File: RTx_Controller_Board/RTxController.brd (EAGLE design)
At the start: 101.6 x 85.5 mm, 79 parts, among them U1 TPD4S014, X3 MINI-USB-32005-301

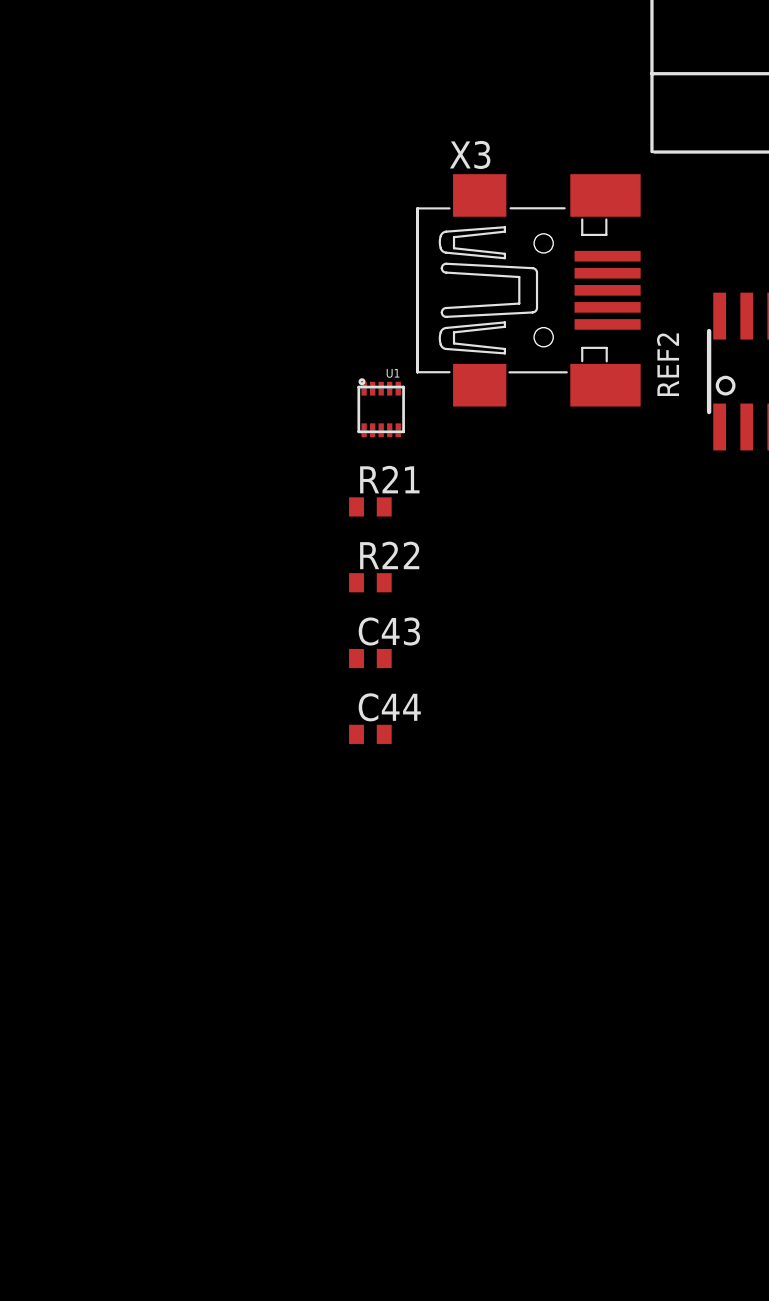
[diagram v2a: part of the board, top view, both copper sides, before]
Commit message: Initial check-in of datasheet for USB ESD protection (better component selected). Updated USB in hardware to incorperate new esd chip.
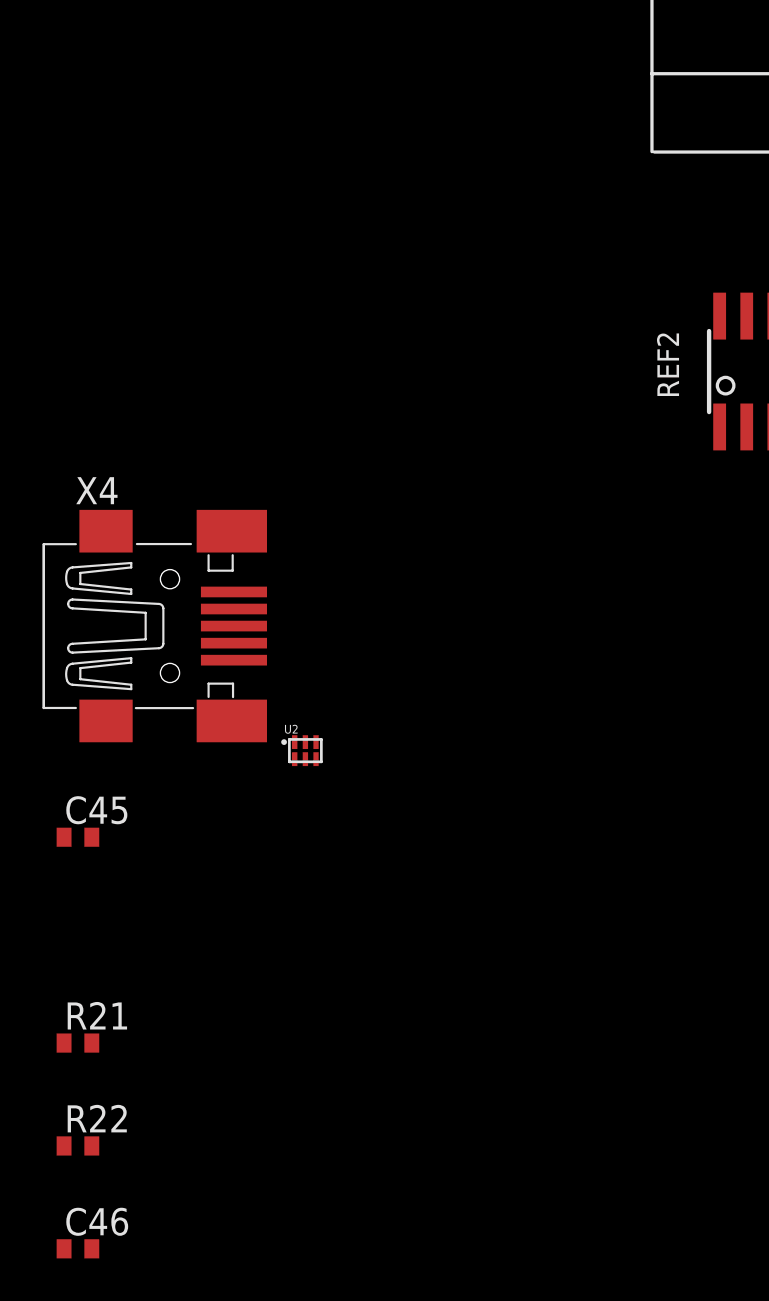
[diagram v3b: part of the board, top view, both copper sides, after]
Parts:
- removed C43, C44: 10u, rcl:C0402
- removed U1: TPD4S014, rtx:TPD4S014
- removed X3: MINI-USB-32005-301, con-cypressindustries:32005-301
- added C45, C46: 10u, rcl:C0402
- added U2: TPD4S012, rtx:TPD4S012
- added X4: MINI-USB-32005-301, con-cypressindustries:32005-301
- moved R22 29.8 mm to (-26.7, -142.5)
- moved R21 28.6 mm to (-26.7, -137.7)
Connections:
- removed net PA9/VBUS: C44.1, U1.1
- new net PA10/ID: U2.3, X4.4
- new net PA9/BBUS: C45.1, C46.1, U2.6, X4.1
- net +5V: no longer C43.1, U1.9, X3.1
- net D+: now also R22.1, U2.1, X4.2; no longer R21.1, U1.7, X3.2
- net D-: now also R21.1, U2.2, X4.3; no longer R22.1, U1.6, X3.3
- net GND: now also C45.2, C46.2, U2.4, X4.5; no longer C43.2, C44.2, U1.5, U1.8, X3.4, X3.5
- net PA11/D-: now also R21.2; no longer R22.2
- net PA12/D+: now also R22.2; no longer R21.2

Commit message: Development of Ethernet PHY.
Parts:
- added C43, C47: 0.1uf 100v, motorFeedback:C0805K
- added C49: 0.1uf, motorFeedback:C0805K
- added D1: SMAJ58A, diode:SMBJ
- added D2: MMBD6050LT1SOT23, motorFeedback:SOT23-TO-236
- added F1: 1A, special:FUSE
- added IC1: LTC4263, motorFeedback:S14-NARROW
- added IC2: TLK110", motorFeedback:LQFP48
- added L1: 10mH, 21mA, motorFeedback:0204V
- added LED1: (no value), motorFeedback:LED5MM
- added R_LED: 1k, motorFeedback:R0603
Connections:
- new net 48VDC+: C43.1, D1.C, D2.3, F1.1, IC1.11, LED1.A
- new net 48VDC-: C43.2, C49.2, IC1.2, IC1.3, IC1.4, IC1.5, IC1.6, IC1.7
- new net AGND: IC2.19
- new net AGND_: IC2.15
- new net AVDD33: IC2.22
- new net DGND: IC2.36
- new net IOGND: IC2.47
- new net IOGND_: IC2.35
- new net N$15: C49.1, IC1.12, IC1.13, IC1.14
- new net N$23: L1.2, LED1.K
- new net N$24: D2.1, L1.1, R_LED.2
- new net N$25: IC1.1, R_LED.1
- new net PORT_MAGNETICS+: C47.1, F1.2
- new net PORT_MAGNETICS-: C47.2, D1.A, IC1.10, IC1.9
- new net VDD_IO: IC2.48
- new net VDD_IO_: IC2.32
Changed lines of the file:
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@@
 <layer number="97" name="Info" color="7" fill="1" visible="no" active="no"/>
 <layer number="98" name="Guide" color="6" fill="1" visible="no" active="no"/>
+<layer number="99" name="SpiceOrder" color="5" fill="1" visible="no" active="no"/>
 <layer number="100" name="Muster" color="7" fill="1" visible="no" active="no"/>
 <layer number="101" name="Patch_Top" color="12" fill="4" visible="yes" active="yes"/>
@@
 <element name="R22" library="rcl" package="R0402" value="22" x="-26.67" y="-142.494"/>
 <element name="C46" library="rcl" package="C0402" value="10u" x="-26.67" y="-147.32"/>
+<element name="IC1" library="motorFeedback" package="S14-NARROW" value="LTC4263" x="-32.258" y="-187.96"/>
+<element name="IC2" library="motorFeedback" package="LQFP48" value="TLK110&quot;" x="-41.656" y="-187.706"/>
+<element name="D1" library="diode" package="SMBJ" value="SMAJ58A" x="-52.324" y="-190.246"/>
+<element name="F1" library="special" package="FUSE" value="1A" x="-41.656" y="-200.406"/>
+<element name="C47" library="motorFeedback" package="C0805K" value="0.1uf 100v" x="-53.594" y="-208.534"/>
+<element name="C49" library="motorFeedback" package="C0805K" value="0.1uf" x="-53.594" y="-218.186"/>
+<element name="L1" library="motorFeedback" package="0204V" value="10mH, 21mA" x="-52.578" y="-223.52"/>
+<element name="LED1" library="motorFeedback" package="LED5MM" value="" x="-51.816" y="-228.346"/>
+<element name="R_LED" library="motorFeedback" package="R0603" value="1k" x="-53.594" y="-233.934"/>
+<element name="D2" library="motorFeedback" package="SOT23-TO-236" value="MMBD6050LT1SOT23" x="-59.436" y="-231.14"/>
+<element name="C43" library="motorFeedback" package="C0805K" value="0.1uf 100v" x="-59.944" y="-238.76"/>
 </elements>
 <signals>
@@
 <wire x1="-19.352" y1="-118.91" x2="-15.502" y2="-123.552" width="0" layer="19" extent="1-1"/>
 </signal>
+<signal name="IOGND">
+<contactref element="IC2" pad="47"/>
+</signal>
+<signal name="VDD_IO">
+<contactref element="IC2" pad="48"/>
+</signal>
+<signal name="AGND_">
+<contactref element="IC2" pad="15"/>
+</signal>
+<signal name="AGND">
+<contactref element="IC2" pad="19"/>
+</signal>
+<signal name="AVDD33">
+<contactref element="IC2" pad="22"/>
+</signal>
+<signal name="VDD_IO_">
+<contactref element="IC2" pad="32"/>
+</signal>
+<signal name="IOGND_">
+<contactref element="IC2" pad="35"/>
+</signal>
+<signal name="DGND">
+<contactref element="IC2" pad="36"/>
+</signal>
+<signal name="N$15">
+<contactref element="IC1" pad="12"/>
+<contactref element="IC1" pad="13"/>
+<contactref element="IC1" pad="14"/>
+<contactref element="C49" pad="1"/>
+<wire x1="-29.278" y1="-185.42" x2="-29.278" y2="-186.69" width="0" layer="19" extent="1-1"/>
+<wire x1="-29.278" y1="-184.15" x2="-29.278" y2="-185.42" width="0" layer="19" extent="1-1"/>
+<wire x1="-54.594" y1="-218.186" x2="-29.278" y2="-186.69" width="0" layer="19" extent="1-1"/>
+</signal>
+<signal name="PORT_MAGNETICS-">
+<contactref element="IC1" pad="10"/>
+<contactref element="IC1" pad="9"/>
+<contactref element="D1" pad="A"/>
+<contactref element="C47" pad="2"/>
+<wire x1="-52.594" y1="-208.534" x2="-50.284" y2="-190.246" width="0" layer="19" extent="1-1"/>
+<wire x1="-29.278" y1="-190.5" x2="-50.284" y2="-190.246" width="0" layer="19" extent="1-1"/>
+<wire x1="-29.278" y1="-189.23" x2="-29.278" y2="-190.5" width="0" layer="19" extent="1-1"/>
+</signal>
+<signal name="48VDC-">
+<contactref element="IC1" pad="2"/>
+<contactref element="IC1" pad="7"/>
+<contactref element="IC1" pad="6"/>
+<contactref element="IC1" pad="5"/>
+<contactref element="IC1" pad="4"/>
+<contactref element="IC1" pad="3"/>
+<contactref element="C49" pad="2"/>
+<contactref element="C43" pad="2"/>
+<wire x1="-35.238" y1="-190.5" x2="-35.238" y2="-191.77" width="0" layer="19" extent="1-1"/>
+<wire x1="-35.238" y1="-189.23" x2="-35.238" y2="-190.5" width="0" layer="19" extent="1-1"/>
+<wire x1="-35.238" y1="-187.96" x2="-35.238" y2="-189.23" width="0" layer="19" extent="1-1"/>
+<wire x1="-35.238" y1="-186.69" x2="-35.238" y2="-187.96" width="0" layer="19" extent="1-1"/>
+<wire x1="-35.238" y1="-185.42" x2="-35.238" y2="-186.69" width="0" layer="19" extent="1-1"/>
+<wire x1="-52.594" y1="-218.186" x2="-35.238" y2="-191.77" width="0" layer="19" extent="1-1"/>
+<wire x1="-58.944" y1="-238.76" x2="-52.594" y2="-218.186" width="0" layer="19" extent="1-1"/>
+</signal>
+<signal name="48VDC+">
+<contactref element="D1" pad="C"/>
+<contactref element="F1" pad="1"/>
+<contactref element="IC1" pad="11"/>
+<contactref element="D2" pad="3"/>
+<contactref element="LED1" pad="A"/>
+<contactref element="C43" pad="1"/>
+<wire x1="-54.354" y1="-190.246" x2="-53.086" y2="-200.406" width="0" layer="19" extent="1-1"/>
+<wire x1="-29.278" y1="-187.96" x2="-54.354" y2="-190.246" width="0" layer="19" extent="1-1"/>
+<wire x1="-53.086" y1="-228.346" x2="-53.086" y2="-200.406" width="0" layer="19" extent="1-1"/>
+<wire x1="-59.436" y1="-230.14" x2="-53.086" y2="-228.346" width="0" layer="19" extent="1-1"/>
+<wire x1="-60.944" y1="-238.76" x2="-59.436" y2="-230.14" width="0" layer="19" extent="1-1"/>
+</signal>
+<signal name="PORT_MAGNETICS+">
+<contactref element="F1" pad="2"/>
+<contactref element="C47" pad="1"/>
+<wire x1="-54.594" y1="-208.534" x2="-30.226" y2="-200.406" width="0" layer="19" extent="1-1"/>
+</signal>
+<signal name="N$24">
+<contactref element="L1" pad="1"/>
+<contactref element="R_LED" pad="2"/>
+<contactref element="D2" pad="1"/>
+<wire x1="-52.744" y1="-233.934" x2="-60.386" y2="-232.14" width="0" layer="19" extent="1-1"/>
+<wire x1="-53.848" y1="-223.52" x2="-52.744" y2="-233.934" width="0" layer="19" extent="1-1"/>
+</signal>
+<signal name="N$25">
+<contactref element="R_LED" pad="1"/>
+<contactref element="IC1" pad="1"/>
+<wire x1="-54.444" y1="-233.934" x2="-35.238" y2="-184.15" width="0" layer="19" extent="1-1"/>
+</signal>
+<signal name="N$23">
+<contactref element="L1" pad="2"/>
+<contactref element="LED1" pad="K"/>
+<wire x1="-50.546" y1="-228.346" x2="-51.308" y2="-223.52" width="0" layer="19" extent="1-1"/>
+</signal>
 </signals>

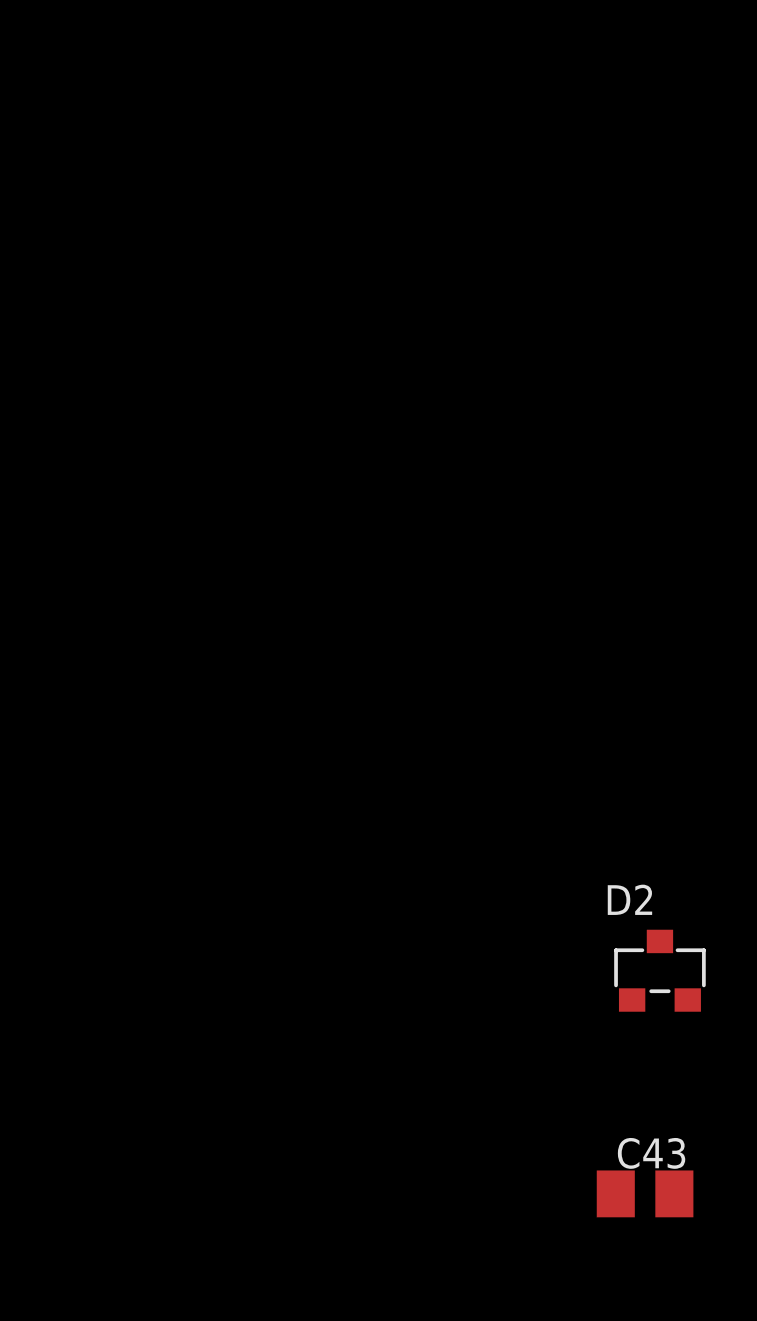
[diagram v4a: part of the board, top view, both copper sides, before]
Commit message: Added MagJack port to Eagle library.
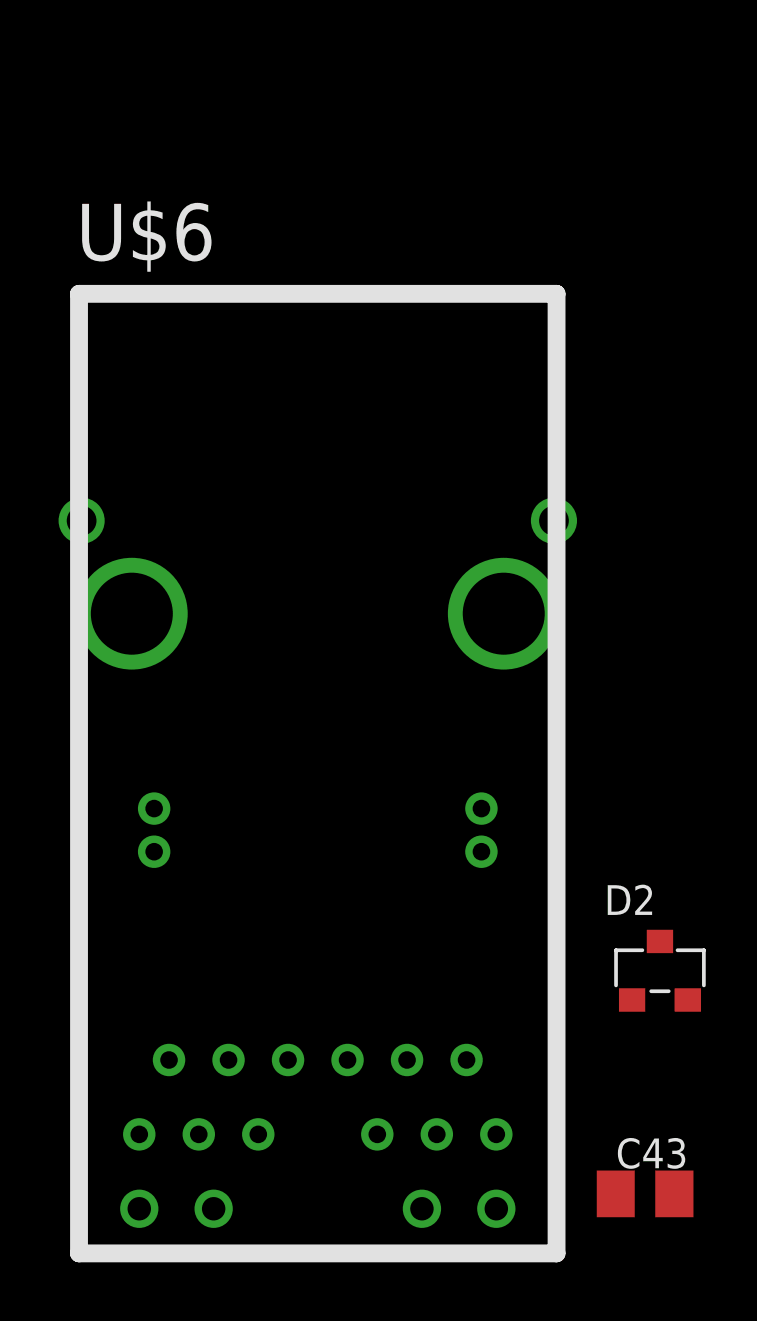
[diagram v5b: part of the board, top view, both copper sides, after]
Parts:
- added U$6: 0826-1X1T-GJ-F, motorFeedback:MAGJACK-RJ45
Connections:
- net PORT_MAGNETICS+: now also U$6.15
- net PORT_MAGNETICS-: now also U$6.16
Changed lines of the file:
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@@
 <element name="D2" library="motorFeedback" package="SOT23-TO-236" value="MMBD6050LT1SOT23" x="-59.436" y="-231.14"/>
 <element name="C43" library="motorFeedback" package="C0805K" value="0.1uf 100v" x="-59.944" y="-238.76"/>
+<element name="U$6" library="motorFeedback" package="MAGJACK-RJ45" value="0826-1X1T-GJ-F" x="-71.12" y="-218.948"/>
 </elements>
 <signals>
@@
 <contactref element="D1" pad="A"/>
 <contactref element="C47" pad="2"/>
+<contactref element="U$6" pad="16"/>
 <wire x1="-52.594" y1="-208.534" x2="-50.284" y2="-190.246" width="0" layer="19" extent="1-1"/>
 <wire x1="-29.278" y1="-190.5" x2="-50.284" y2="-190.246" width="0" layer="19" extent="1-1"/>
 <wire x1="-29.278" y1="-189.23" x2="-29.278" y2="-190.5" width="0" layer="19" extent="1-1"/>
+<wire x1="-65.532" y1="-225.6028" x2="-52.594" y2="-208.534" width="0" layer="19" extent="1-1"/>
 </signal>
 <signal name="48VDC-">
@@
 <contactref element="F1" pad="2"/>
 <contactref element="C47" pad="1"/>
+<contactref element="U$6" pad="15"/>
 <wire x1="-54.594" y1="-208.534" x2="-30.226" y2="-200.406" width="0" layer="19" extent="1-1"/>
+<wire x1="-76.708" y1="-225.6028" x2="-54.594" y2="-208.534" width="0" layer="19" extent="1-1"/>
 </signal>
 <signal name="N$24">

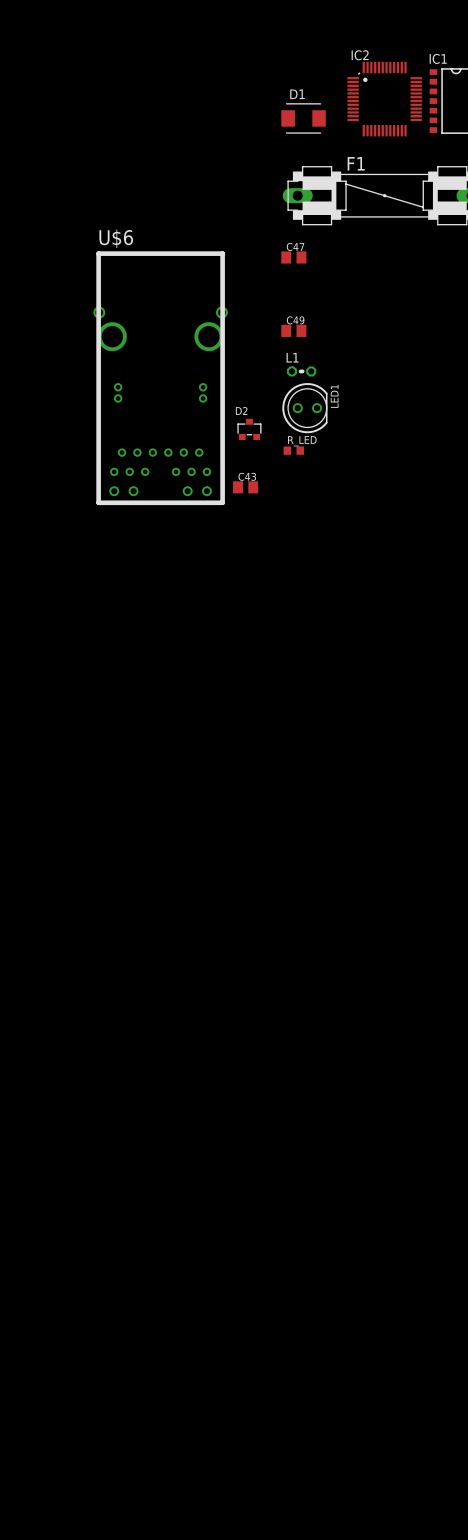
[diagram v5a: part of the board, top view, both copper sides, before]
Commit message: Updated Ethernet PHY components and schematic.
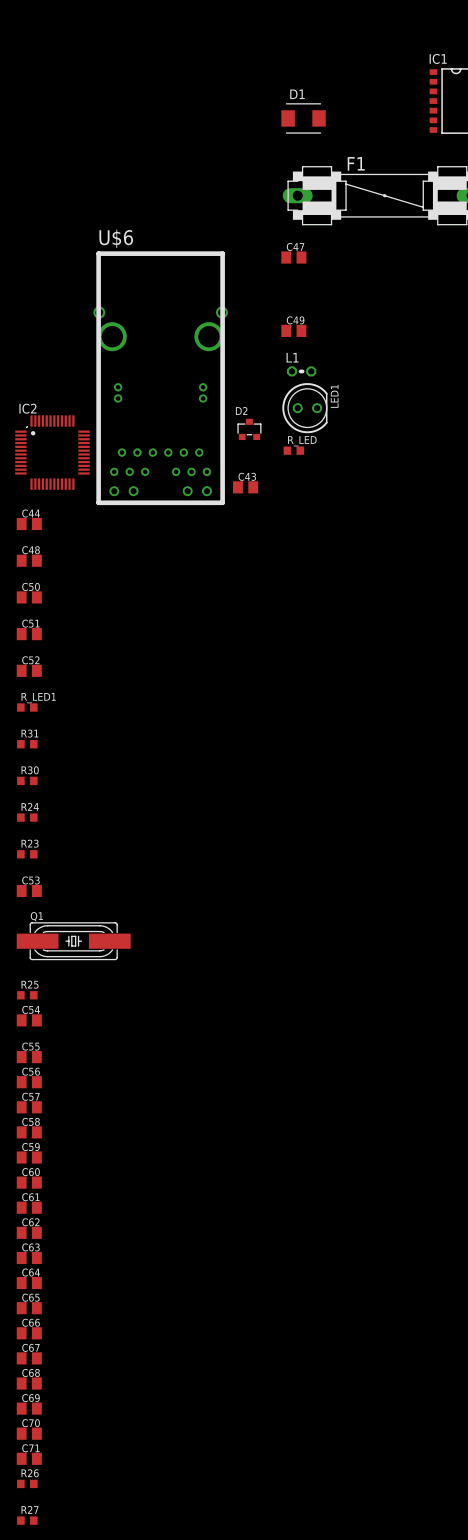
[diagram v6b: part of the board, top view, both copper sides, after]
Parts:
- added C44, C50, C52, C53: 1u, motorFeedback:C0805K
- added C48, C51: 0.1u, motorFeedback:C0805K
- added C54, C55, C56, C57, C58, C59, C60, C61, C62, C63, C64, C65, C66, C67, C68, C69, C70, C71: (no value), motorFeedback:C0805K
- added Q1: 25MHz, motorFeedback:CSM-7X
- added R23, R31, R_LED1: 1k, motorFeedback:R0603
- added R24, R30: 49.9, motorFeedback:R0603
- added R25: (no value), motorFeedback:R0603
- added R26: 4.87k, motorFeedback:R0603
- added R27: 2.2k, motorFeedback:R0603
- C43, C47: value 0.1uf 100v -> 0.1u 100v
- L1: value 10mH, 21mA -> 10m, 21mA
- moved IC2 63.8 mm to (-85.3, -234.2)
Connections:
- removed net AGND: IC2.19
- removed net AGND_: IC2.15
- removed net AVDD33: IC2.22
- removed net DGND: IC2.36
- removed net IOGND: IC2.47
- removed net IOGND_: IC2.35
- removed net VDD_IO: IC2.48
- removed net VDD_IO_: IC2.32
- new net N$26: IC2.17, R23.2, U$6.11
- new net N$27: IC2.16, R24.1, U$6.10
- new net N$28: IC2.14, R31.2, U$6.4
- new net N$29: IC2.13, R30.1, U$6.5
- new net N$30: C53.1, R23.1, R24.2
- new net N$31: IC2.33, R25.2
- new net N$32: C55.1, IC2.34, Q1.1
- new net N$33: C54.1, Q1.2, R25.1
- new net N$34: IC2.20, R27.2
- new net N$40: IC2.24, R26.2
- new net N$41: C68.2, C69.2, C70.2, C71.2, IC2.18, IC2.23, IC2.37
- net +3.3V: now also C44.1, C48.1, C50.1, C51.1, C52.1, C56.2, C57.2, C58.2, C59.2, C60.2, C61.2, C62.2, C63.2, C64.2, C65.2, C66.2, C67.2, IC2.22, IC2.32, IC2.48, R27.1, R30.2, R31.1, U$6.12, U$6.6
- net GND: now also C44.2, C48.2, C50.2, C51.2, C52.2, C53.2, C54.2, C55.2, C56.1, C57.1, C58.1, C59.1, C60.1, C61.1, C62.1, C63.1, C64.1, C65.1, C66.1, C67.1, C68.1, C69.1, C70.1, C71.1, IC2.15, IC2.19, IC2.35, IC2.36, IC2.47, R26.1
- net N$24: now also R_LED1.2
- net N$25: now also R_LED1.1
